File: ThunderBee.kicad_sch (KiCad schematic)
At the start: 0 parts

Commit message: FPGA MGT
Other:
- added sheet FPGA (FPGA.kicad_sch)
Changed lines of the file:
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@@
 (kicad_sch (version 20230409) (generator eeschema)
-  (paper "A4")
+  (paper "A3")
   (text "——A replica for ThunderScope" (exclude_from_sim no)
  (at 132.715 60.96 0)
@@
       )
     )
+  )
+  (sheet (at 21.59 83.185) (size 67.945 12.7) (fields_autoplaced)
+    (stroke (width 0.1524) (type solid))
+    (fill (color 0 0 0 0.0000))
+    (property "Sheetname" "FPGA" (at 21.59 82.4734 0)
+      (effects (font (size 1.27 1.27)) (justify left bottom))
+    )
+    (property "Sheetfile" "FPGA.kicad_sch" (at 21.59 96.4696 0)
+      (effects (font (size 1.27 1.27)) (justify left top))
+    )
+    (instances
+      (project "ThunderBee"
+        (path "/0304beac-e45e-4f64-b366-6bc6d40756cf" (page "3"))
+      )
+    )

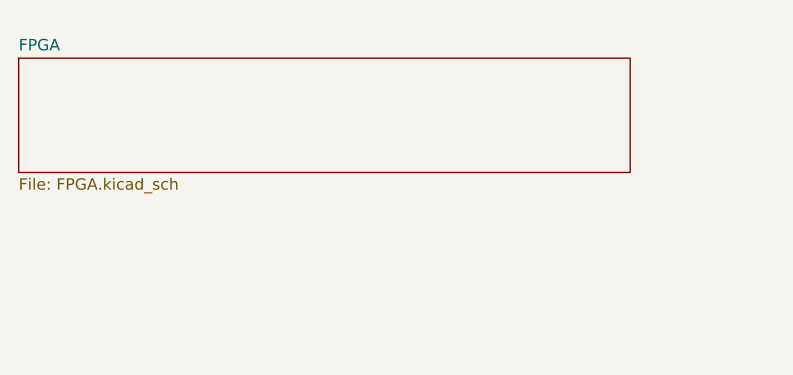
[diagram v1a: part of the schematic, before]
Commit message: DDR Labels
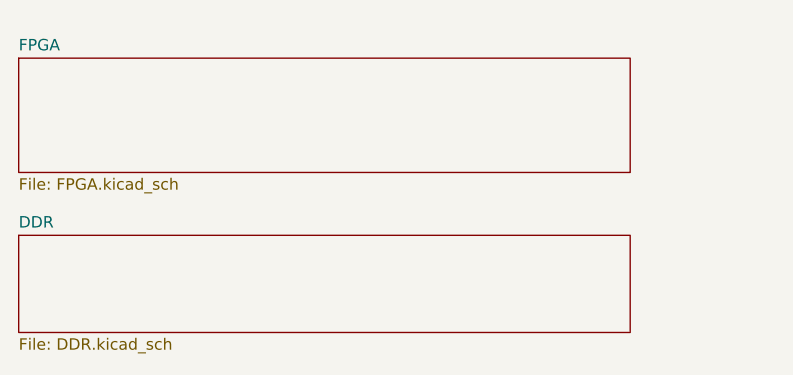
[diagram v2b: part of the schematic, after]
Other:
- added sheet DDR (DDR.kicad_sch)
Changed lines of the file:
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@@
+    )
+  )
+  (sheet (at 21.59 102.87) (size 67.945 10.795) (fields_autoplaced)
+    (stroke (width 0.1524) (type solid))
+    (fill (color 0 0 0 0.0000))
+    (property "Sheetname" "DDR" (at 21.59 102.1584 0)
+      (effects (font (size 1.27 1.27)) (justify left bottom))
+    )
+    (property "Sheetfile" "DDR.kicad_sch" (at 21.59 114.2496 0)
+      (effects (font (size 1.27 1.27)) (justify left top))
+    )
+    (instances
+      (project "ThunderBee"
+        (path "/0304beac-e45e-4f64-b366-6bc6d40756cf" (page "4"))
+      )
     )
   )
